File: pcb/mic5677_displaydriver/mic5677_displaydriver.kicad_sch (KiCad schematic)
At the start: 81 parts, among them J1 Segment DIP14, J2 Segment DIP14, J3 Segment Wire Connector, J4 Common Cathode Enable, J5 PSU, J6 Bypass, J7 Serial Debug, J8 8P8C, Q1 D45H8G, Q10 BC546, Q11 BC546, Q12 BC546, Q13 BC546, Q14 BC546, Q15 BC546, Q16 BC546, Q17 BC546, Q18 BC546, Q19 BC546, Q2 D45H8G, Q20 BC546, Q21 BC546, Q22 BC546, Q23 BC546, Q3 D45H8G, Q4 D45H8G, Q5 D45H8G, Q6 D45H8G, Q7 D45H8G, Q8 D45H8G, Q9 D45H8G, U1 L7805, U2 74HC595, U3 74HC595, U4 74HC02

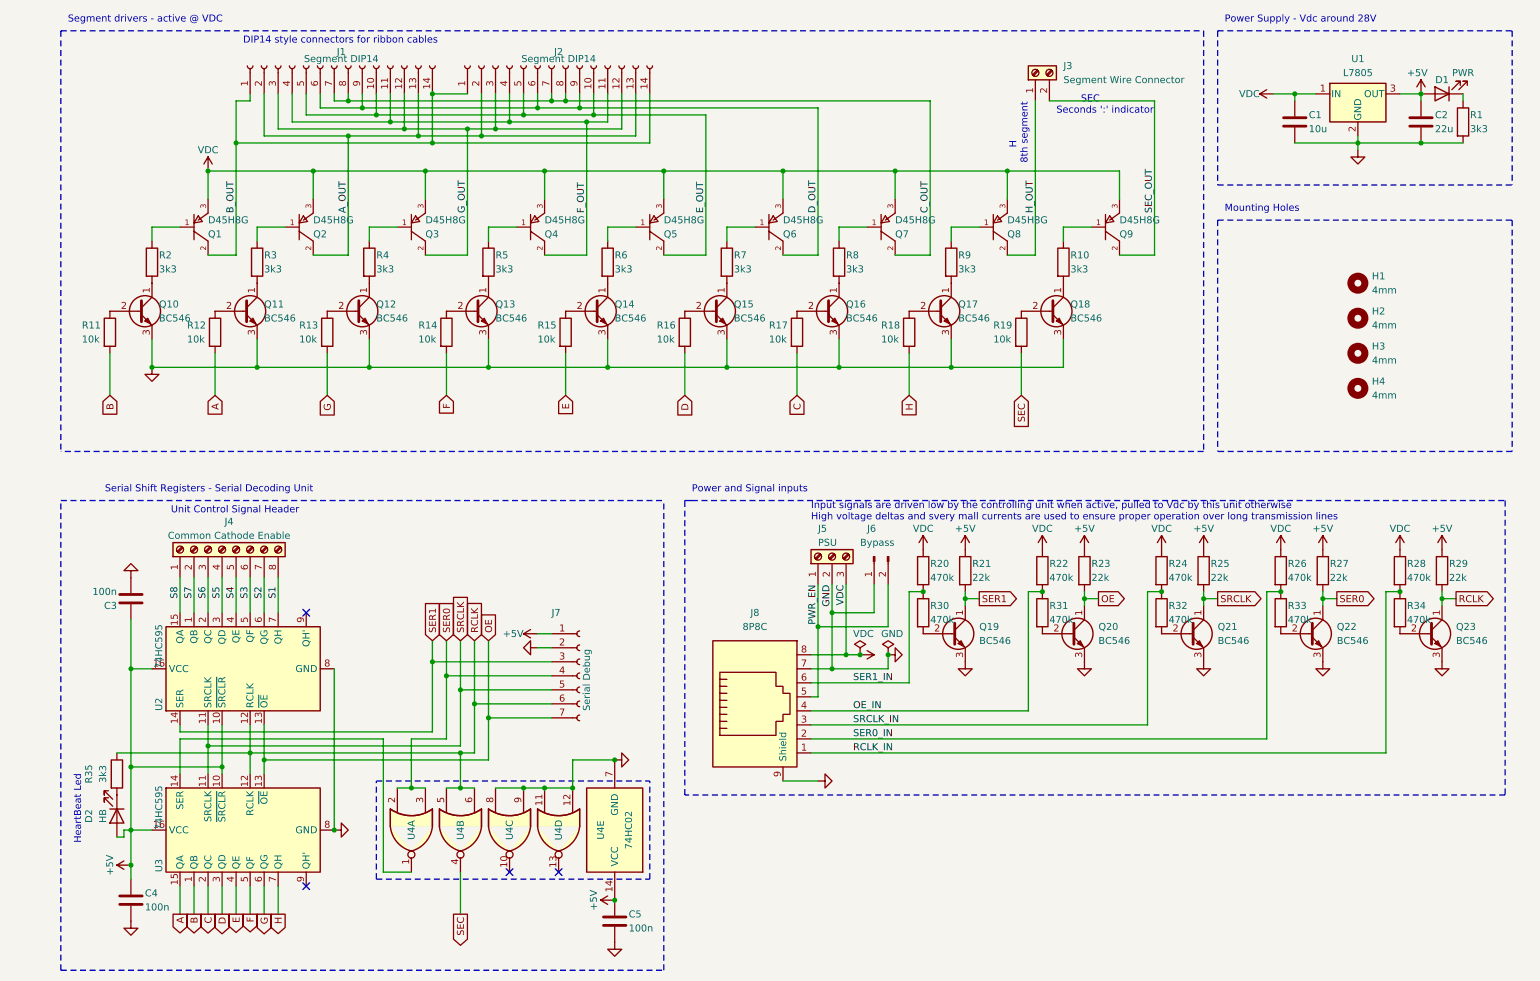
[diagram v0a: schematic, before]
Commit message: Moved ddriver HB led, adopted better 8p8c pinout, improved fill zones
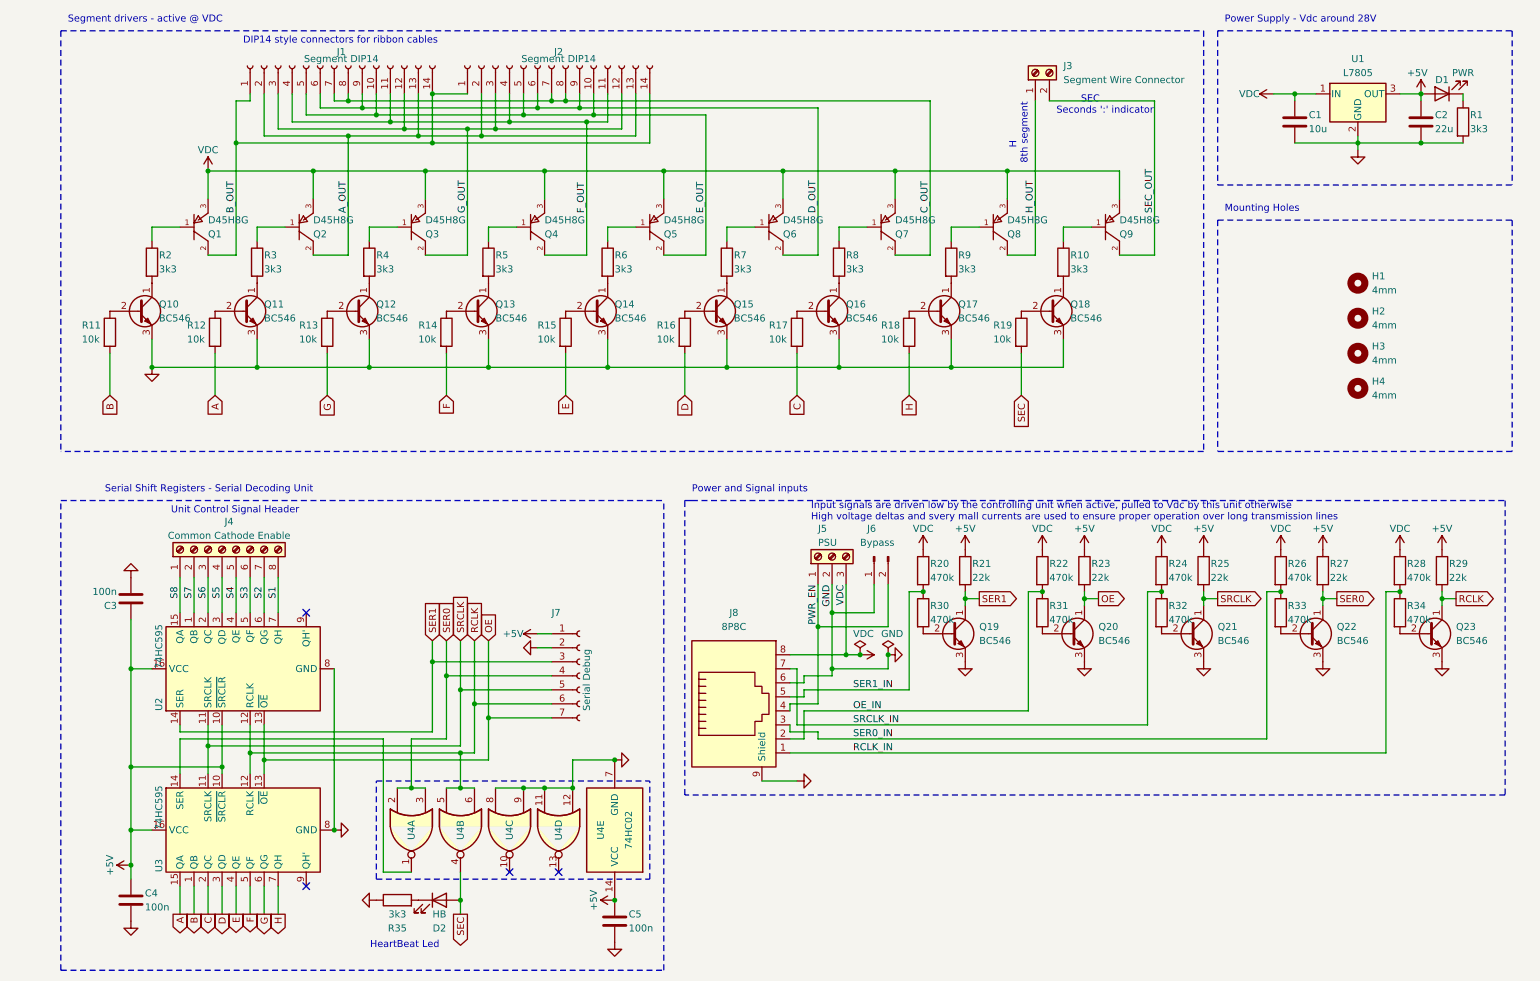
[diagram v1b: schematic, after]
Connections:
- net +5V: no longer D2.2 (A)
- net GND: now also J8.6, R35.1; no longer J8.7
- net OE_IN: now also J8.2; no longer J8.4
- net PWR_EN: now also J8.4; no longer J8.5
- net RCLK: no longer R35.1
- net SEC: now also D2.2 (A)
- net SER0_IN: now also J8.3; no longer J8.2
- net SER1_IN: now also J8.5; no longer J8.6
- net SRCLK_IN: now also J8.7; no longer J8.3
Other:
- moved on the sheet: D2, J8, R35
